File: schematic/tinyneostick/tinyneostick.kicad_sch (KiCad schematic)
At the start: 18 parts, among them J1 Conn_01x03, J2 Conn_01x03

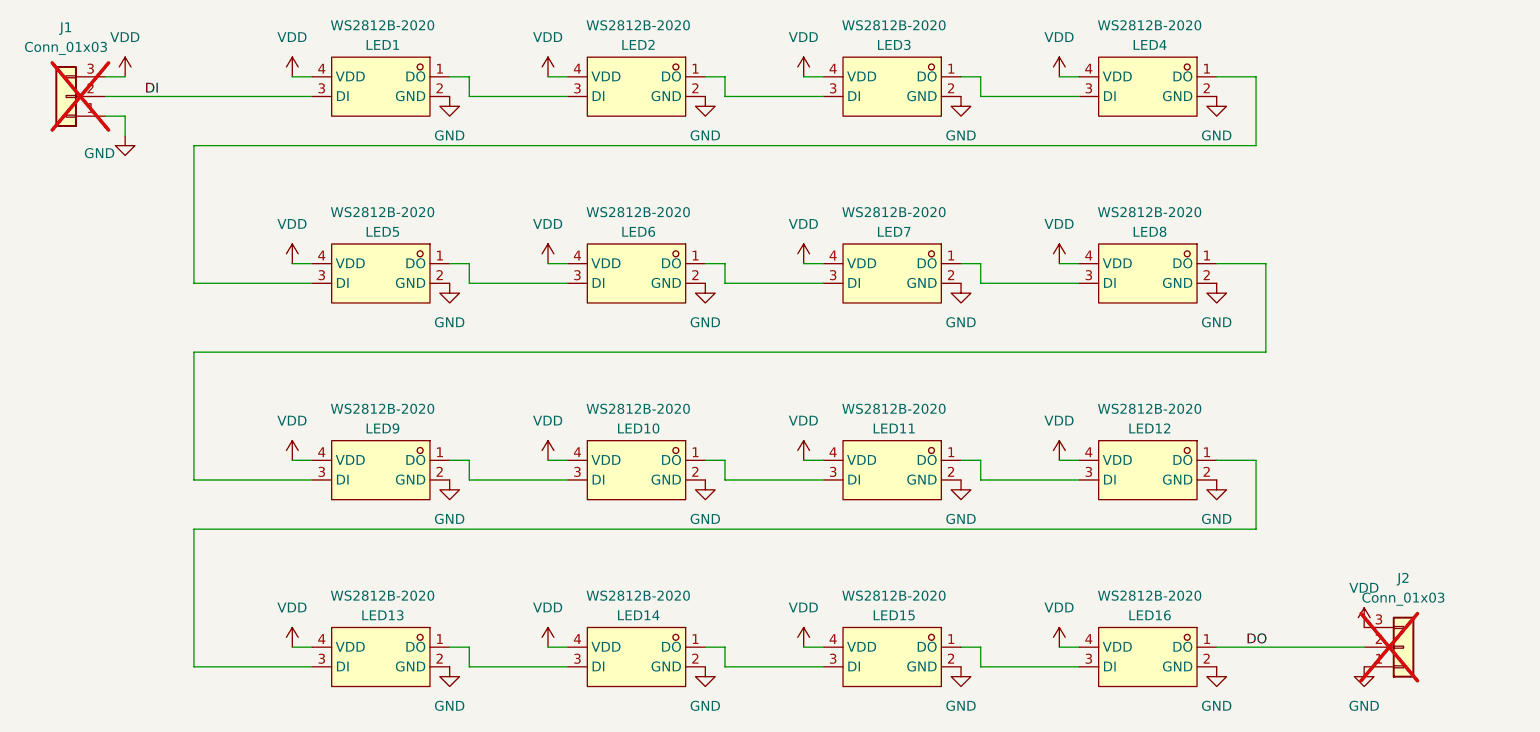
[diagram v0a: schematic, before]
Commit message: smd version, 48mm x 7.8mm, cannot be PCBAd by JLC tho
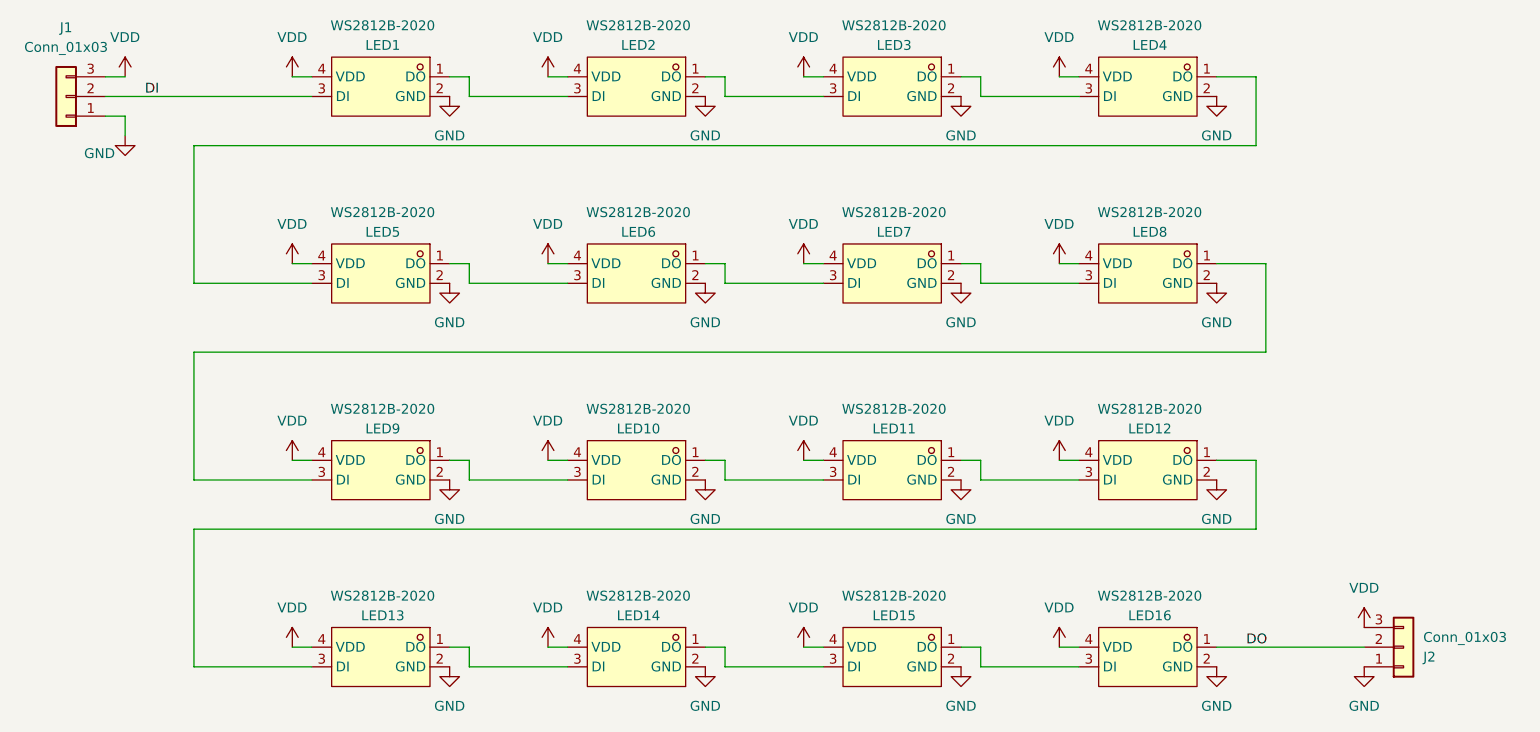
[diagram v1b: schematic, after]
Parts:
- J1, J2: footprint Connector_PinHeader_2.54mm:PinHeader_1x03_P2.54mm_Vertical -> todbot_stuff:Pins_1x03_P2.54mm_Horizontal_SMT; now fitted
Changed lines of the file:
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@@
+	)
+	(symbol
+		(lib_id "PCM_4ms_Connector:Conn_01x03")
+		(at 246.38 129.54 0)
+		(mirror x)
+		(unit 1)
+		(exclude_from_sim no)
+		(in_bom no)
+		(on_board yes)
+		(dnp no)
+		(property "Reference" "J2"
+			(at 248.92 130.8101 0)
+			(effects
+				(font
+					(size 1.27 1.27)
+				)
+				(justify left)
+			)
+		)
+		(property "Value" "Conn_01x03"
+			(at 248.92 128.2701 0)
+			(effects
+				(font
+					(size 1.27 1.27)
+				)
+				(justify left)
+			)
+		)
+		(property "Footprint" "todbot_stuff:Pins_1x03_P2.54mm_Horizontal_SMT"
+			(at 246.38 136.525 0)
+			(effects
+				(font
+					(size 1.27 1.27)
+				)
+				(hide yes)
+			)
+		)
+		(property "Datasheet" ""
+			(at 246.38 129.54 0)
+			(effects
+				(font
+					(size 1.27 1.27)
+				)
+				(hide yes)
+			)
+		)
+		(property "Description" "HEADER 1x3 MALE PINS 0.100” 180deg"
+			(at 246.38 129.54 0)
+			(effects
+				(font
+					(size 1.27 1.27)
+				)
+				(hide yes)
+			)
+		)
+		(property "Specifications" "HEADER 1x3 MALE PINS 0.100” 180deg"
+			(at 243.84 121.666 0)
+			(effects
+				(font
+					(size 1.27 1.27)
+				)
+				(justify left)
+				(hide yes)
+			)
+		)
+		(property "Manufacturer" "TAD"
+			(at 243.84 120.142 0)
+			(effects
+				(font
+					(size 1.27 1.27)
+				)
+				(justify left)
+				(hide yes)
+			)
+		)
+		(property "Part Number" "1-0301FBV0T"
+			(at 243.84 118.618 0)
+			(effects
+				(font
+					(size 1.27 1.27)
+				)
+				(justify left)
+				(hide yes)
+			)
+		)
+		(property "LCSC Part" ""
+			(at 246.38 129.54 0)
+			(effects
+				(font
+					(size 1.27 1.27)
+				)
+				(hide yes)
+			)
+		)
+		(property "DigikeyPN" ""
+			(at 246.38 129.54 0)
+			(effects
+				(font
+					(size 1.27 1.27)
+				)
+				(hide yes)
+			)
+		)
+		(property "MPN" ""
+			(at 246.38 129.54 0)
+			(effects
+				(font
+					(size 1.27 1.27)
+				)
+				(hide yes)
+			)
+		)
+		(property "Note" ""
+			(at 246.38 129.54 0)
+			(effects
+				(font
+					(size 1.27 1.27)
+				)
+			)
+		)
+		(pin "1"
+		)
+		(pin "2"
+		)
+		(pin "3"
+		)
+		(instances
+			(project "tinyneostick"
+				(path "/39765a13-7678-4446-b76c-43af02a394d2"
+					(reference "J2")
+					(unit 1)
+				)
+			)
+		)
 	)
 	(symbol
@@
 	)
 	(symbol
-		(lib_id "PCM_4ms_Connector:Conn_01x03")
-		(at 246.38 129.54 0)
-		(mirror x)
-		(unit 1)
-		(exclude_from_sim no)
-		(in_bom no)
-		(on_board yes)
-		(dnp yes)
-		(property "Reference" "J2"
-			(at 246.38 120.65 0)
-			(effects
-				(font
-					(size 1.27 1.27)
-				)
-			)
-		)
-		(property "Value" "Conn_01x03"
-			(at 246.38 123.19 0)
-			(effects
-				(font
-					(size 1.27 1.27)
-				)
-			)
-		)
-		(property "Footprint" "Connector_PinHeader_2.54mm:PinHeader_1x03_P2.54mm_Vertical"
-			(at 246.38 136.525 0)
-			(effects
-				(font
-					(size 1.27 1.27)
-				)
-				(hide yes)
-			)
-		)
-		(property "Datasheet" ""
-			(at 246.38 129.54 0)
-			(effects
-				(font
-					(size 1.27 1.27)
-				)
-				(hide yes)
-			)
-		)
-		(property "Description" "HEADER 1x3 MALE PINS 0.100” 180deg"
-			(at 246.38 129.54 0)
-			(effects
-				(font
-					(size 1.27 1.27)
-				)
-				(hide yes)
-			)
-		)
-		(property "Specifications" "HEADER 1x3 MALE PINS 0.100” 180deg"
-			(at 243.84 121.666 0)
-			(effects
-				(font
-					(size 1.27 1.27)
-				)
-				(justify left)
-				(hide yes)
-			)
-		)
-		(property "Manufacturer" "TAD"
-			(at 243.84 120.142 0)
-			(effects
-				(font
-					(size 1.27 1.27)
-				)
-				(justify left)
-				(hide yes)
-			)
-		)
-		(property "Part Number" "1-0301FBV0T"
-			(at 243.84 118.618 0)
-			(effects
-				(font
-					(size 1.27 1.27)
-				)
-				(justify left)
-				(hide yes)
-			)
-		)
-		(property "LCSC Part" ""
-			(at 246.38 129.54 0)
-			(effects
-				(font
-					(size 1.27 1.27)
-				)
-				(hide yes)
-			)
-		)
-		(property "DigikeyPN" ""
-			(at 246.38 129.54 0)
-			(effects
-				(font
-					(size 1.27 1.27)
-				)
-				(hide yes)
-			)
-		)
-		(property "MPN" ""
-			(at 246.38 129.54 0)
-			(effects
-				(font
-					(size 1.27 1.27)
-				)
-				(hide yes)
-			)
-		)
-		(property "Note" ""
-			(at 246.38 129.54 0)
-			(effects
-				(font
-					(size 1.27 1.27)
-				)
-			)
-		)
-		(pin "1"
-		)
-		(pin "2"
-		)
-		(pin "3"
-		)
-		(instances
-			(project "tinyneostick"
-				(path "/39765a13-7678-4446-b76c-43af02a394d2"
-					(reference "J2")
-					(unit 1)
-				)
-			)
-		)
-	)
-	(symbol
 		(lib_id "power:VDD")
 		(at 201.93 55.88 0)
@@
 		(in_bom no)
 		(on_board yes)
-		(dnp yes)
+		(dnp no)
 		(fields_autoplaced yes)
 		(property "Reference" "J1"
@@
 			)
 		)
-		(property "Footprint" "Connector_PinHeader_2.54mm:PinHeader_1x03_P2.54mm_Vertical"
+		(property "Footprint" "todbot_stuff:Pins_1x03_P2.54mm_Horizontal_SMT"
 			(at 73.66 65.405 0)
 			(effects

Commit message: small fixes
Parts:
- J1, J2: footprint todbot_stuff:Pins_1x03_P2.54mm_Horizontal_SMT -> todbot_stuff:Pins_1x03_P2.54mm_Horizontal_SMT_bigger
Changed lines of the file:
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@@
 			)
 		)
-		(property "Footprint" "todbot_stuff:Pins_1x03_P2.54mm_Horizontal_SMT"
+		(property "Footprint" "todbot_stuff:Pins_1x03_P2.54mm_Horizontal_SMT_bigger"
 			(at 246.38 136.525 0)
 			(effects
@@
 			)
 		)
-		(property "Footprint" "todbot_stuff:Pins_1x03_P2.54mm_Horizontal_SMT"
+		(property "Footprint" "todbot_stuff:Pins_1x03_P2.54mm_Horizontal_SMT_bigger"
 			(at 73.66 65.405 0)
 			(effects
